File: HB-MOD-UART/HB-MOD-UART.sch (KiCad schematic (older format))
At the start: 8 parts, among them J1 Conn_Raspi, J2 Conn_Coaxial, U1 HM-MOD-UART

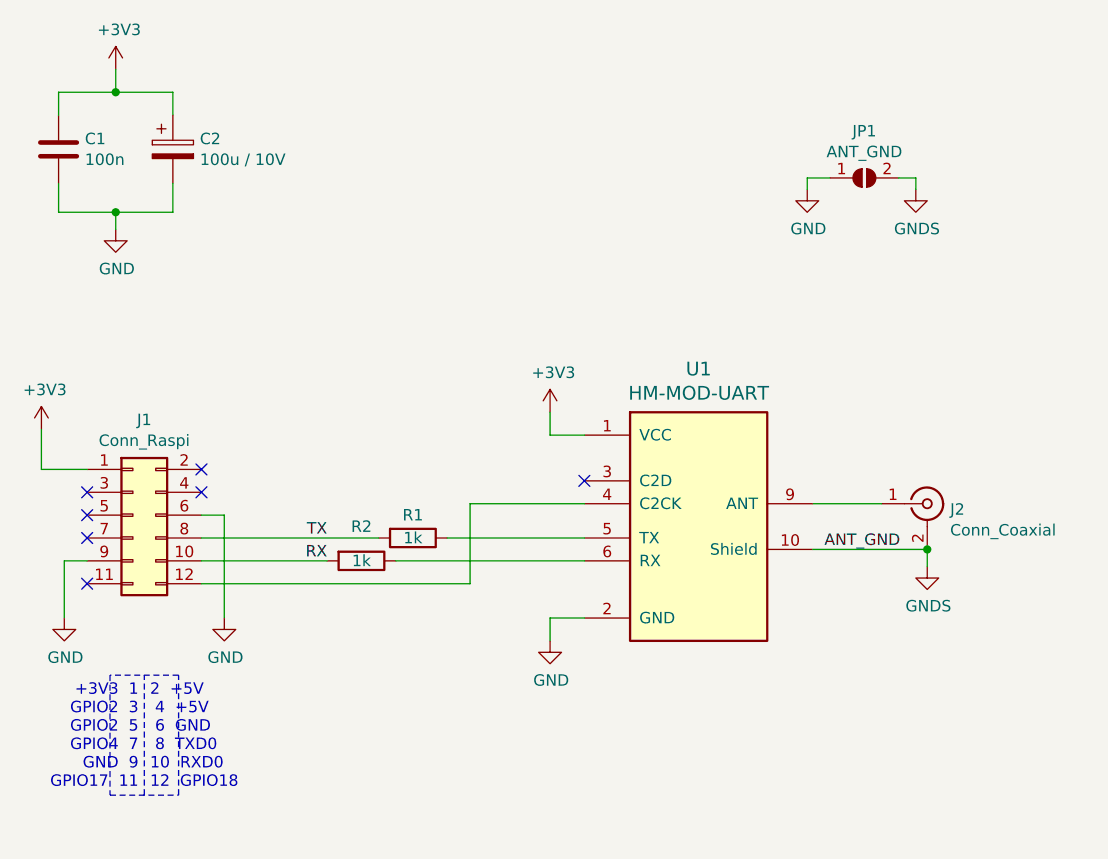
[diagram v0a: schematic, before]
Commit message: HB-MOD-UART: swap RX/TX
fixes #3
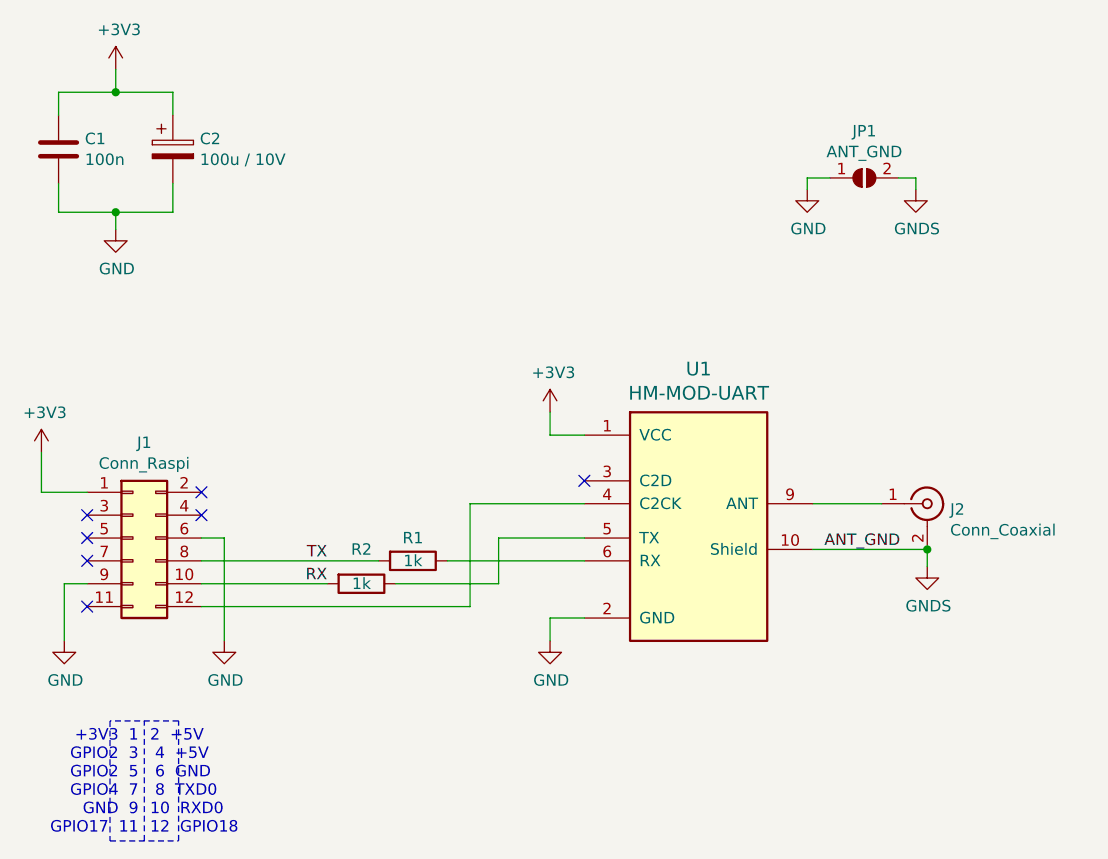
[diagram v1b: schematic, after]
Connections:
- net at U1.5 (TX): now also R2.1; no longer R1.1
- net at U1.6 (RX): now also R1.1; no longer R2.1
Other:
- moved on the sheet: J1, R1, R2
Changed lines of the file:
@@
 Title "HB-MOD-UART"
 Date "Nov 2019"
-Rev "1.0"
+Rev "1.1"
 Comp ""
-Comment1 ""
+Comment1 "V1.1: RX/TX swapped"
 Comment2 ""
 Comment3 ""
@@
 L Connector_Generic:Conn_02x06_Odd_Even J1
 U 1 1 5DC18A31
-P 3150 3925
-F 0 "J1" H 3200 4342 50  0000 C CNN
-F 1 "Conn_Raspi" H 3200 4251 50  0000 C CNN
-F 2 "Pin_Headers:Pin_Header_Straight_2x06_Pitch2.54mm" H 3150 3925 50  0001 C CNN
-F 3 "~" H 3150 3925 50  0001 C CNN
-	1    3150 3925
+P 3150 4025
+F 0 "J1" H 3200 4442 50  0000 C CNN
+F 1 "Conn_Raspi" H 3200 4351 50  0000 C CNN
+F 2 "Pin_Headers:Pin_Header_Straight_2x06_Pitch2.54mm" H 3150 4025 50  0001 C CNN
+F 3 "~" H 3150 4025 50  0001 C CNN
+	1    3150 4025
 	1    0    0    -1
 $EndComp
@@
 L power:+3V3 #PWR02
 U 1 1 5DC1958D
-P 2750 3550
-F 0 "#PWR02" H 2750 3400 50  0001 C CNN
-F 1 "+3V3" H 2765 3723 50  0000 C CNN
-F 2 "" H 2750 3550 50  0001 C CNN
-F 3 "" H 2750 3550 50  0001 C CNN
-	1    2750 3550
-	1    0    0    -1
-$EndComp
-Wire Wire Line
-	2750 3725 2750 3550
-Wire Wire Line
-	2750 3725 2950 3725
-NoConn ~ 2950 3825
+P 2750 3650
+F 0 "#PWR02" H 2750 3500 50  0001 C CNN
+F 1 "+3V3" H 2765 3823 50  0000 C CNN
+F 2 "" H 2750 3650 50  0001 C CNN
+F 3 "" H 2750 3650 50  0001 C CNN
+	1    2750 3650
+	1    0    0    -1
+$EndComp
+Wire Wire Line
+	2750 3825 2750 3650
+Wire Wire Line
+	2750 3825 2950 3825
 NoConn ~ 2950 3925
 NoConn ~ 2950 4025
-NoConn ~ 2950 4225
-NoConn ~ 3450 3725
+NoConn ~ 2950 4125
+NoConn ~ 2950 4325
 NoConn ~ 3450 3825
-Text Label 4000 4025 2    50   ~ 0
+NoConn ~ 3450 3925
+Text Label 4000 4125 2    50   ~ 0
 TX
-Text Label 4000 4125 2    50   ~ 0
+Text Label 4000 4225 2    50   ~ 0
 RX
 $Comp
 L power:GND #PWR05
 U 1 1 5DC1B10E
-P 3550 4375
-F 0 "#PWR05" H 3550 4125 50  0001 C CNN
-F 1 "GND" H 3555 4202 50  0000 C CNN
-F 2 "" H 3550 4375 50  0001 C CNN
-F 3 "" H 3550 4375 50  0001 C CNN
-	1    3550 4375
-	1    0    0    -1
-$EndComp
-Wire Wire Line
-	3550 4375 3550 3925
-Wire Wire Line
-	3550 3925 3450 3925
+P 3550 4475
+F 0 "#PWR05" H 3550 4225 50  0001 C CNN
+F 1 "GND" H 3555 4302 50  0000 C CNN
+F 2 "" H 3550 4475 50  0001 C CNN
+F 3 "" H 3550 4475 50  0001 C CNN
+	1    3550 4475
+	1    0    0    -1
+$EndComp
+Wire Wire Line
+	3550 4475 3550 4025
+Wire Wire Line
+	3550 4025 3450 4025
 $Comp
 L power:GND #PWR07
@@
 L power:GND #PWR04
 U 1 1 5DC1D117
-P 2850 4375
-F 0 "#PWR04" H 2850 4125 50  0001 C CNN
-F 1 "GND" H 2855 4202 50  0000 C CNN
-F 2 "" H 2850 4375 50  0001 C CNN
-F 3 "" H 2850 4375 50  0001 C CNN
-	1    2850 4375
-	1    0    0    -1
-$EndComp
-Wire Wire Line
-	2850 4375 2850 4125
-Wire Wire Line
-	2850 4125 2950 4125
+P 2850 4475
+F 0 "#PWR04" H 2850 4225 50  0001 C CNN
+F 1 "GND" H 2855 4302 50  0000 C CNN
+F 2 "" H 2850 4475 50  0001 C CNN
+F 3 "" H 2850 4475 50  0001 C CNN
+	1    2850 4475
+	1    0    0    -1
+$EndComp
+Wire Wire Line
+	2850 4475 2850 4225
+Wire Wire Line
+	2850 4225 2950 4225
 Wire Wire Line
 	4975 3475 4975 3575
-Text Notes 3175 5125 2    50   ~ 0
+Text Notes 3175 5325 2    50   ~ 0
 +3V3  1 \nGPIO2  3 \nGPIO2  5 \nGPIO4  7 \nGND  9 \nGPIO17  11
-Text Notes 3225 5125 0    50   ~ 0
+Text Notes 3225 5325 0    50   ~ 0
  2  +5V\n 4  +5V\n 6  GND\n 8  TXD0\n10  RXD0\n12  GPIO18
 Wire Notes Line
-	3350 5150 3350 4625
-Wire Notes Line
-	3350 4625 3050 4625
-Wire Notes Line
-	3050 4625 3050 5150
-Wire Notes Line
-	3200 5150 3200 4625
-Wire Notes Line
-	3050 5150 3350 5150
-Wire Wire Line
-	3450 4225 4625 4225
-Wire Wire Line
-	4625 4225 4625 3875
+	3350 5350 3350 4825
+Wire Notes Line
+	3350 4825 3050 4825
+Wire Notes Line
+	3050 4825 3050 5350
+Wire Notes Line
+	3200 5350 3200 4825
+Wire Notes Line
+	3050 5350 3350 5350
+Wire Wire Line
+	3450 4325 4625 4325
 Wire Wire Line
 	4625 3875 5125 3875
@@
 $EndComp
 Wire Wire Line
-	3450 4025 4225 4025
-Wire Wire Line
-	4000 4125 3450 4125
+	3450 4125 4225 4125
+Wire Wire Line
+	4000 4225 3450 4225
 $Comp
 L Device:R R1
 U 1 1 5DC41A77
-P 4375 4025
-F 0 "R1" V 4275 4025 50  0000 C CNN
-F 1 "1k" V 4375 4025 50  0000 C CNN
-F 2 "Resistors_SMD:R_0805_HandSoldering" V 4305 4025 50  0001 C CNN
-F 3 "~" H 4375 4025 50  0001 C CNN
-	1    4375 4025
+P 4375 4125
+F 0 "R1" V 4275 4125 50  0000 C CNN
+F 1 "1k" V 4375 4125 50  0000 C CNN
+F 2 "Resistors_SMD:R_0805_HandSoldering" V 4305 4125 50  0001 C CNN
+F 3 "~" H 4375 4125 50  0001 C CNN
+	1    4375 4125
 	0    1    1    0
 $EndComp
@@
 L Device:R R2
 U 1 1 5DC428C9
-P 4150 4125
-F 0 "R2" V 4000 4125 50  0000 C CNN
-F 1 "1k" V 4150 4125 50  0000 C CNN
-F 2 "Resistors_SMD:R_0805_HandSoldering" V 4080 4125 50  0001 C CNN
-F 3 "~" H 4150 4125 50  0001 C CNN
-	1    4150 4125
+P 4150 4225
+F 0 "R2" V 4000 4225 50  0000 C CNN
+F 1 "1k" V 4150 4225 50  0000 C CNN
+F 2 "Resistors_SMD:R_0805_HandSoldering" V 4080 4225 50  0001 C CNN
+F 3 "~" H 4150 4225 50  0001 C CNN
+	1    4150 4225
 	0    1    1    0
 $EndComp
-Wire Wire Line
-	4525 4025 5125 4025
-Wire Wire Line
-	5125 4125 4300 4125
 $Comp
 L power:GND #PWR0101
@@
 Wire Wire Line
 	6125 4075 6625 4075
+Wire Wire Line
+	4625 3875 4625 4325
+Wire Wire Line
+	4525 4125 5125 4125
+Wire Wire Line
+	4300 4225 4750 4225
+Wire Wire Line
+	4750 4225 4750 4025
+Wire Wire Line
+	4750 4025 5125 4025
 $EndSCHEMATC
